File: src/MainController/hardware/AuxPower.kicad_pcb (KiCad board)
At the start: 2 copper layers, 90 x 90 mm, 123 parts, among them J1 MC 1,5/2, J10 MC 1,5/4, J11 S3B-XH-A, J12 S3B-XH-A, J13 S3B-XH-A, J14 S3B-XH-A, J15 S3B-XH-A, J16 B3B-XH-A, J17 B4B-XH-A, J2 MC 1,5/2, J3 MC 1,5/2, J4 MC 1,5/2, J5 MC 1,5/2, J6 MC 1,5/4, J7 MC 1,5/4, J8 MC 1,5/4, J9 MC 1,5/4, Q1 BC846B,235, Q10 AO4421, Q2 BC846B,235, Q3 BC846B,235, Q4 BC846B,235, Q5 BC846B,235, Q6 AO4421, Q7 AO4421, Q8 AO4421, Q9 AO4421, U1 ZXCT1009, U2 ZXCT1009, U3 ZXCT1009, U5 ZXCT1009, U6 PIC18F26K83, U7 PI4IOE5V6416, U8 MCP9701

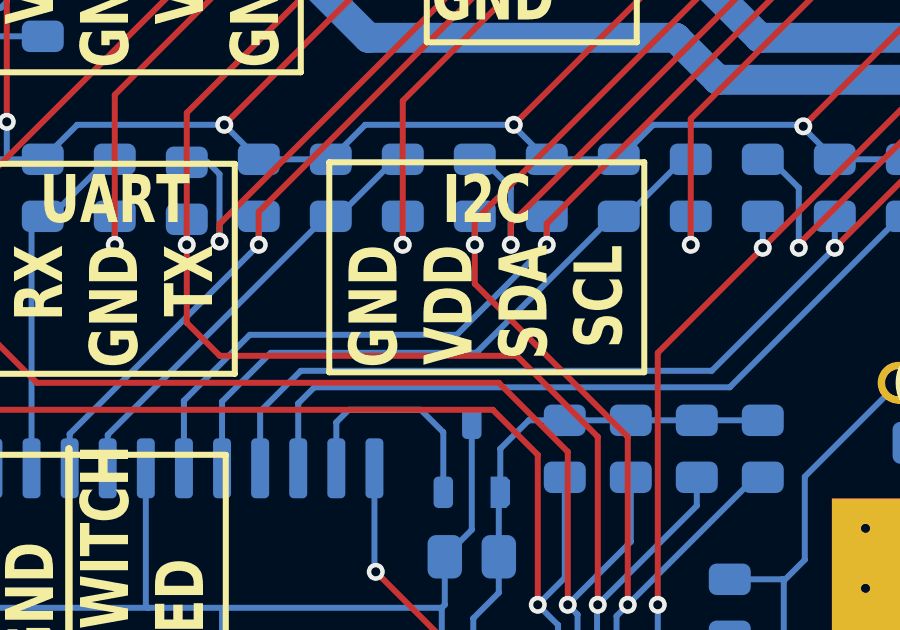
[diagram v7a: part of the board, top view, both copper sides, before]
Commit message: MainController: Updated silkscreen
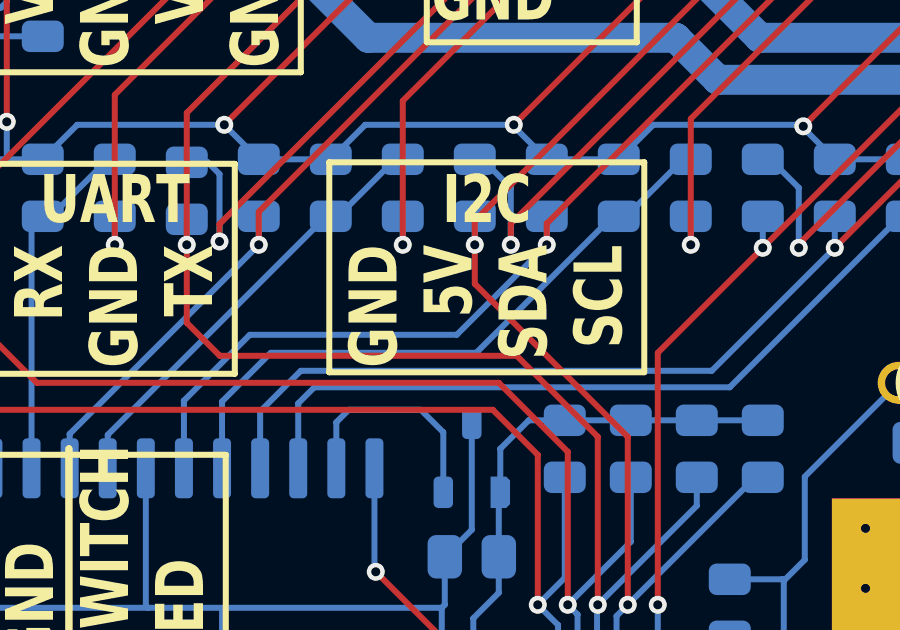
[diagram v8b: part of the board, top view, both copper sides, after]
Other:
- board text removed: "VDD"
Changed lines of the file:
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@@
 		)
 	)
-	(gr_text "VDD"
+	(gr_text "5V"
 		(at 38.75 52.9 90)
 		(layer "F.SilkS")
